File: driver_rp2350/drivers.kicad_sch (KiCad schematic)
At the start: 80 parts, among them U10 UCC27517, U11 UCC27517, U12 UCC27517, U13 UCC27517, U14 UCC27517, U15 UCC27517, U16 UCC27517, U17 UCC27517, U18 UCC27517, U19 UCC27517, U20 UCC27517, U21 UCC27517, U22 UCC27517, U23 UCC27517, U24 UCC27517, U25 UCC27517, U26 UCC27517, U27 UCC27517, U28 UCC27517, U29 UCC27517, U3 UCC27517, U30 UCC27517, U31 UCC27517, U32 UCC27517, U33 UCC27517, U34 UCC27517, U35 UCC27517, U36 UCC27517, U37 UCC27517, U38 UCC27517, U4 UCC27517, U5 UCC27517, U6 UCC27517, U7 UCC27517, U8 UCC27517, U9 UCC27517

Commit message: Worked on modifications for converting rp2350 design to 18x18 array.
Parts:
- C20, C21, C22, C23, C24, C25, C26, C27, C28, C29, C30, C31, C32, C33, C34, C35, C36, C37, C38, C39, C40, C41, C42, C43, C44, C45, C46, C47, C48, C49, C50, C51, C52, C53, C54, C55: footprint Capacitor_SMD:C_0402_1005Metric -> Capacitor_SMD:C_0201_0603Metric
- U10, U11, U12, U13, U14, U15, U16, U17, U18, U19, U20, U21, U22, U23, U24, U25, U26, U27, U28, U29, U3, U30, U31, U32, U33, U34, U35, U36, U37, U38, U4, U5, U6, U7, U8, U9: footprint (none) -> Package_TO_SOT_SMD:SOT-23-5

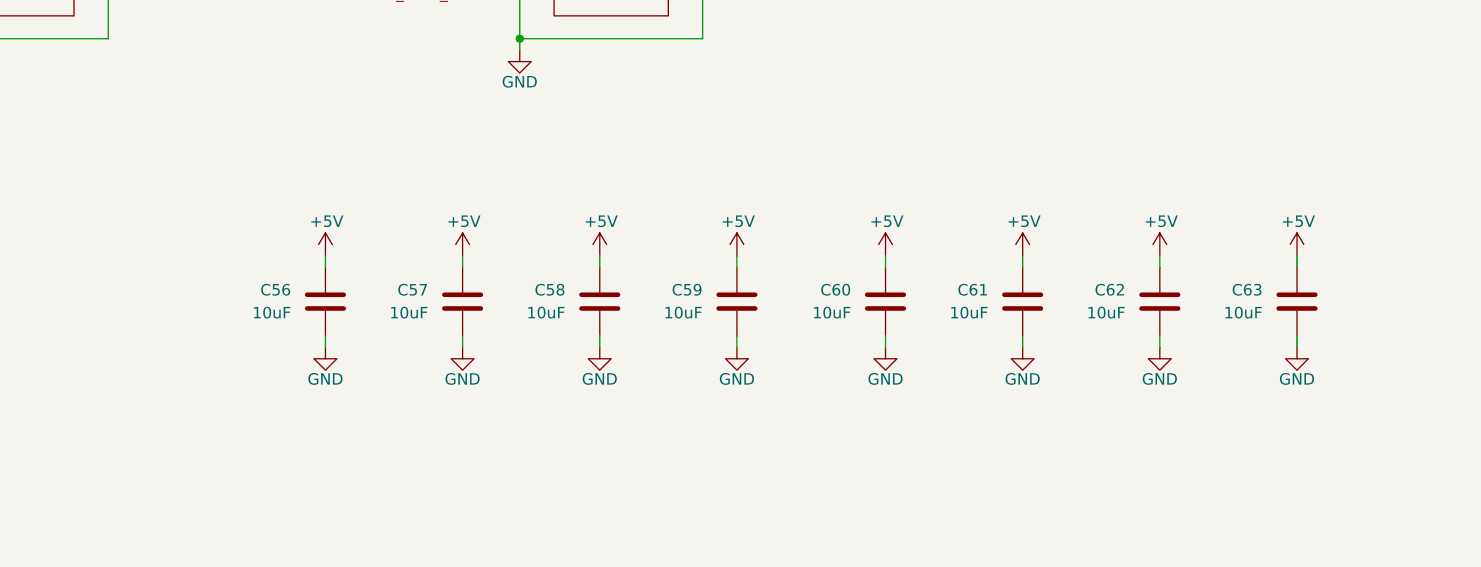
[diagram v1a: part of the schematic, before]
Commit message: Modified for rp2354.
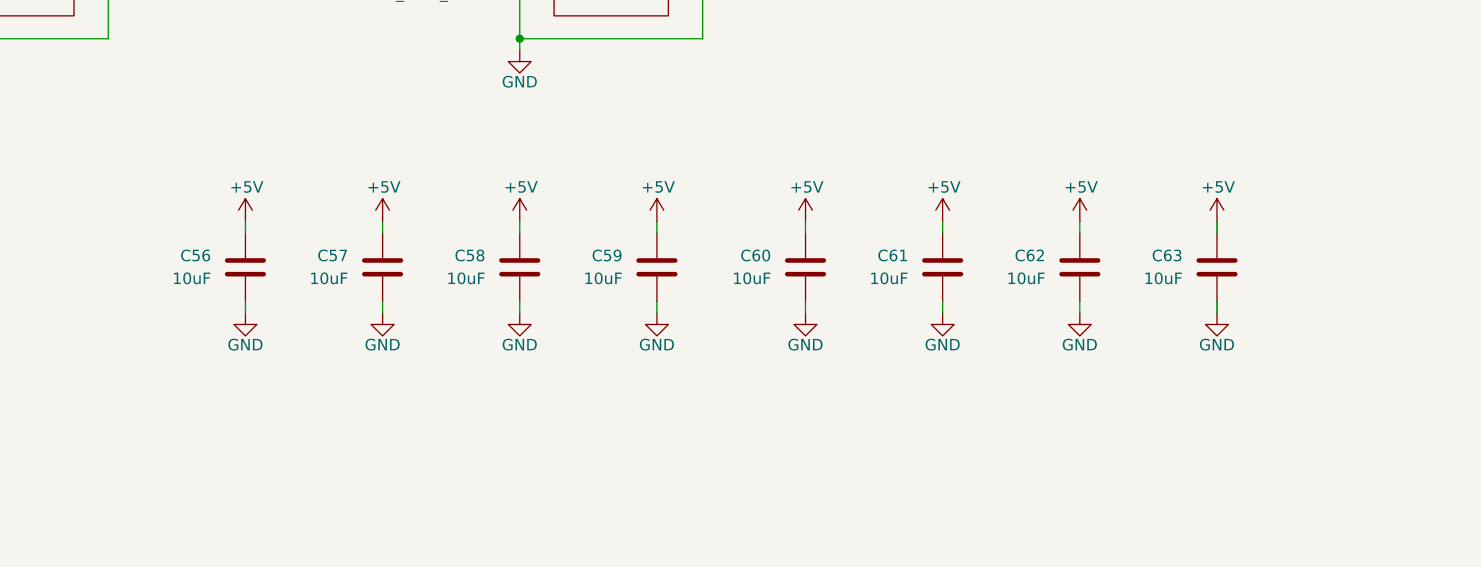
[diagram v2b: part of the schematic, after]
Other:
- moved on the sheet: C56, C57, C58, C59, C60, C61, C62, C63

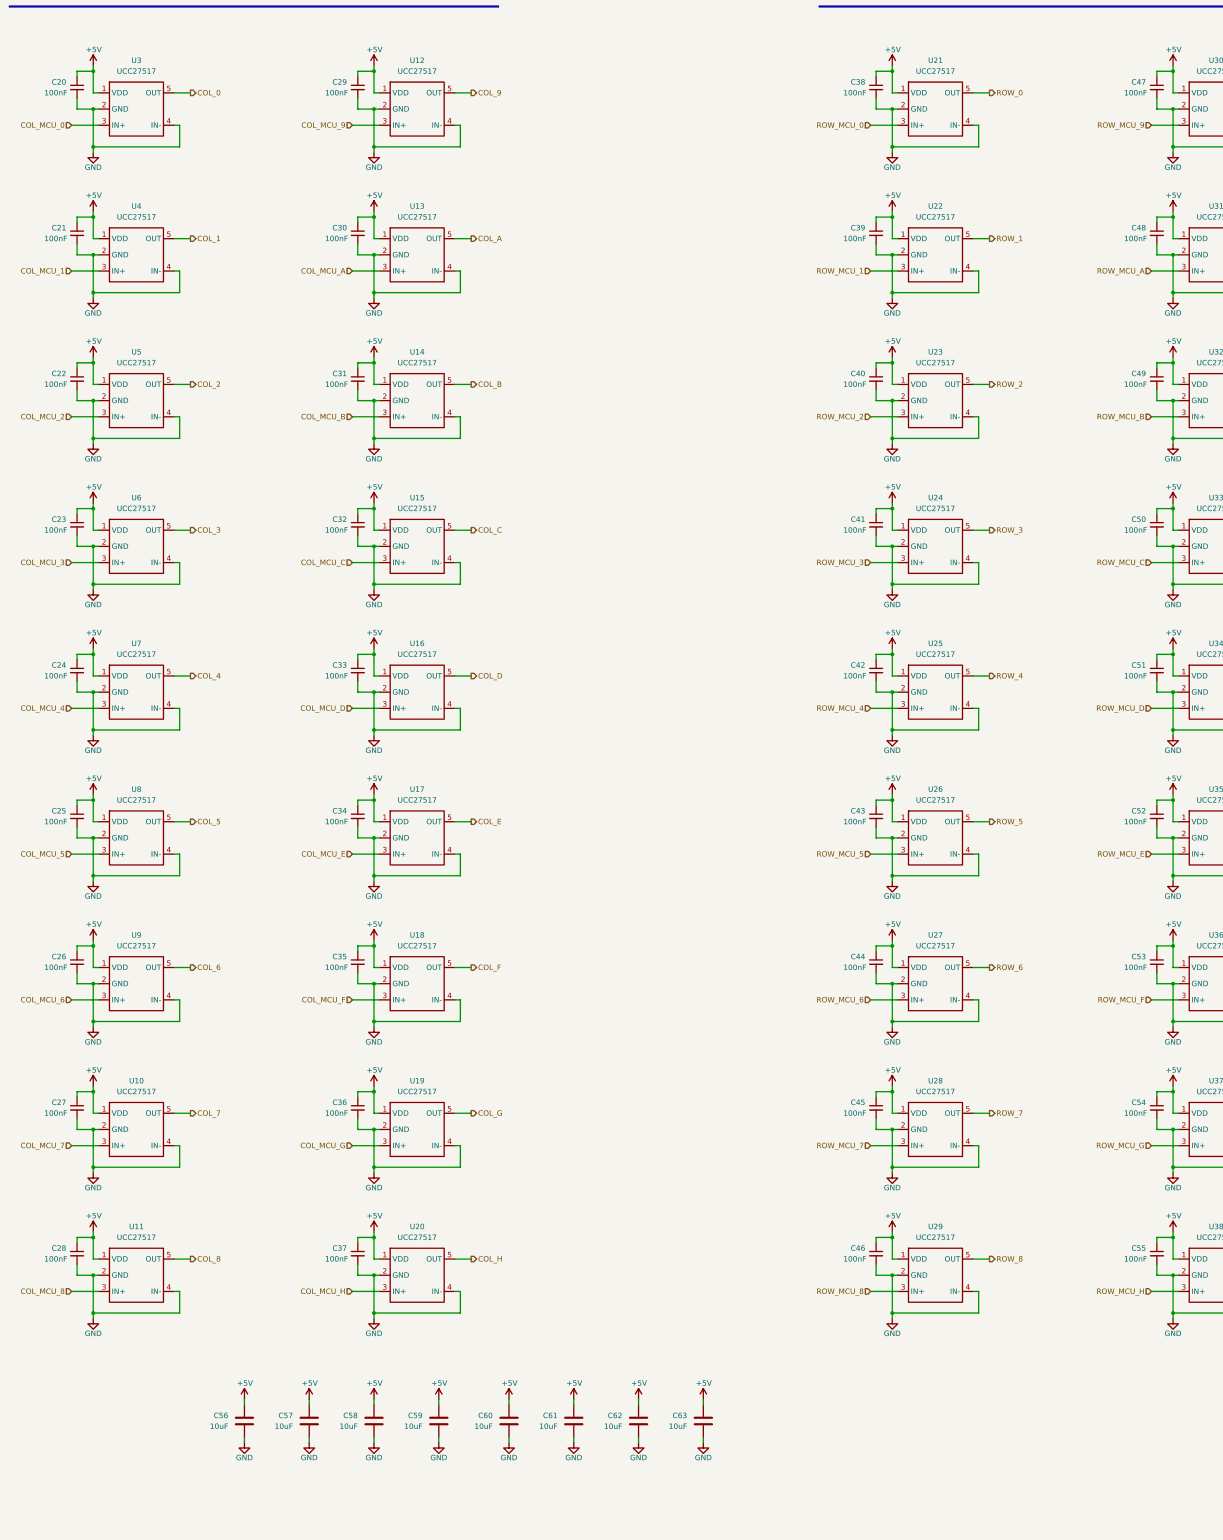
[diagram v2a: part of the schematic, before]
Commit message: Worked on layout for 18x18 rp2354b panels.
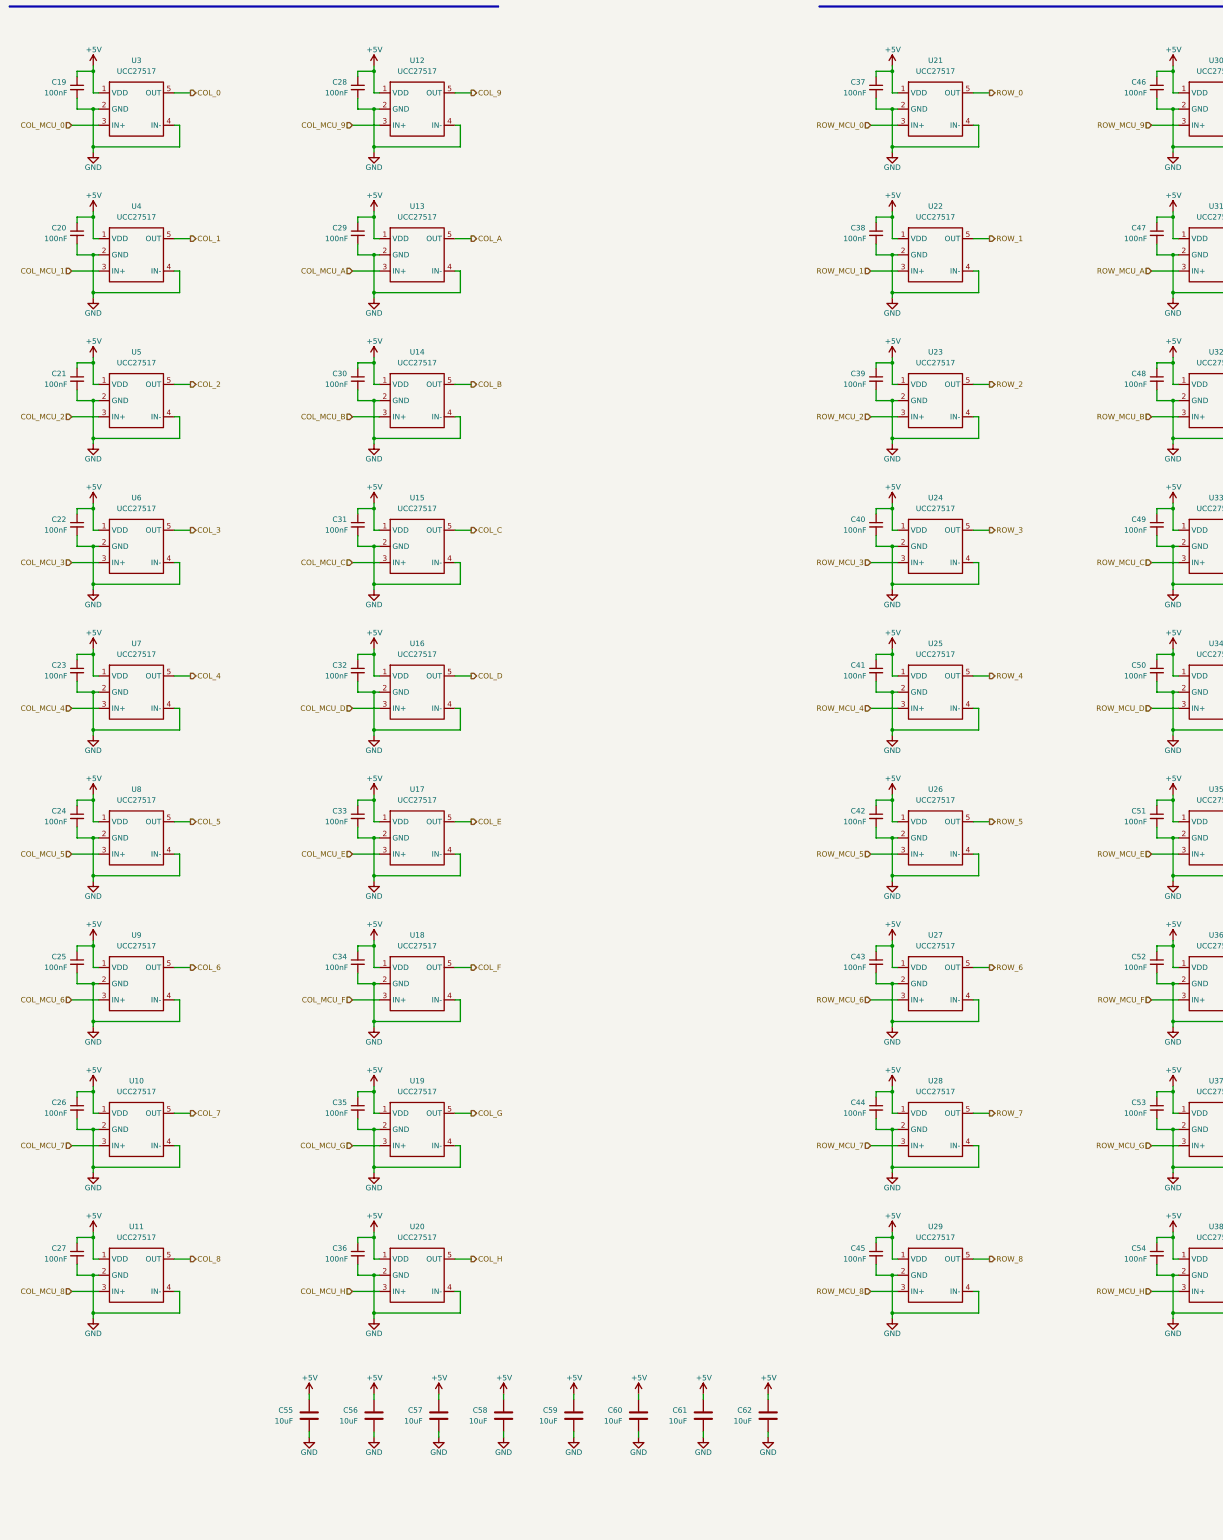
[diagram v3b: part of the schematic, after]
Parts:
- renumbered C20 to C19, C21 to C20, C22 to C21, C23 to C22, C24 to C23, C25 to C24, C26 to C25, C27 to C26, C28 to C27, C29 to C28, C30 to C29, C31 to C30, C32 to C31, C33 to C32, C34 to C33, C35 to C34, C36 to C35, C37 to C36, C38 to C37, C39 to C38, C40 to C39, C41 to C40, C42 to C41, C43 to C42, C44 to C43, C45 to C44, C46 to C45, C47 to C46, C48 to C47, C49 to C48, C50 to C49, C51 to C50, C52 to C51, C53 to C52, C54 to C53, C55 to C54, C56 to C55, C57 to C56, C58 to C57, C59 to C58, C60 to C59, C61 to C60, C62 to C61, C63 to C62
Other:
- moved on the sheet: C55, C56, C57, C58, C59, C60, C61, C62
